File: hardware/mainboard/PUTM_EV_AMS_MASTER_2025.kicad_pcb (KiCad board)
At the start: 4 copper layers, 60 x 100 mm, 236 parts, among them IC1 3.3V/0.5A, IC2 TPS54202HDDCR, IC3 BQ79600PWRQ1, IC4 TLV61046ADBVT, IC6 AMC3330DWER, IC7 AMC3330DWER, IC8 ADC 24bit, IC9 LTC1799, J1 M80-5100642, J10 M300-MV10345M1, J2 M80-5102042, J3 M80-5100842, J4 FTSH-107-01-L-D-K, J5 M80-51004XX, J7 M300-MV10345M1, J8 M80-51004XX, K1 IM07DTS, Q1 DMT6018LDR-7, Q2 DMT6018LDR-7, Q3 DMT6018LDR-7, Q4 SI2347DS-T1-GE3, Q6 2N7002, Q7 DMT6018LDR-7, Q8 2N7002, Q9 2N7002, T1 SM91502ALE, U10 STM32H573RITx, U12 LM393, U13 LM393, U14 LM393, U2 FT230XS, U3 74AUP1G32, U4 TPS2113PWR, U6 MCP2542FD-E/MF, U7 MCP2542FD-E/MF

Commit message: sync
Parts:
- moved TP1 2.25 mm to (139.0, 126.2)
- moved TP4 2.25 mm to (139.0, 128.2)
- moved C47 1.25 mm to (133.8, 88.2)
- moved TP11 1.03 mm to (119.0, 117.0)
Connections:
- J2 pad 12: /CHARGER_DETECTION -> VBUS+
- J2 pad 13: /AIR_P_DETECTION -> /CHARGER_DETECTION
- J2 pad 14: /AIR_PRE_DETECTION -> /AIR_P_DETECTION
- J2 pad 15: /AIR_M_DETECTION -> /AIR_PRE_DETECTION
- J2 pad 16: unconnected-(J2-Pad16) -> /AIR_M_DETECTION
- J2 pad 17: VBUS+ -> +8V
- J2 pad 18: TSMS -> /SAFETY_IN
- J2 pad 7: /SAFETY_OUT -> GND
- J2 pad 8: /SAFETY_IN -> /SAFETY_OUT
- J2 pad 9: +8V -> TSMS
- R49 pad 2: TSMS -> /SDC_AIRS
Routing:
- net /ADC_MOSI: track 0.00 -> 41.1 mm, vias 0 -> 2
- net /~{CS_MISO}: track 0.00 -> 40.5 mm, vias 0 -> 2
- net /ADC_SCK: track 0.00 -> 39.8 mm, vias 0 -> 2
- net /ADC_MISO: track 2.79 -> 42.0 mm, vias 1 -> 2
- net /~{ADC_DRY}: track 0.00 -> 35.4 mm, vias 0 -> 2
- net /UCTX: track 0.00 -> 27.1 mm
- net /UCRX: track 0.00 -> 24.3 mm
- net /ADC/ACU_V-: track 0.00 -> 20.7 mm
- net /~{FLT}: track 7.02 -> 27.7 mm, vias 1 -> 2
- net /UTX: track 0.00 -> 20.6 mm
- net /ADC/ACU_V+: track 0.00 -> 20.6 mm
- net /SDC_AIRS: track 24.1 -> 42.2 mm
- net /URX: track 0.00 -> 16.7 mm
- net /FAN2-: track 4.63 -> 18.9 mm
- net /FAN1-: track 3.47 -> 16.9 mm
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- added copper zone on In2.Cu, net +3.3VA
- added copper zone on In2.Cu, net +3.3VMCU
- added copper zone on In2.Cu, net +5VA

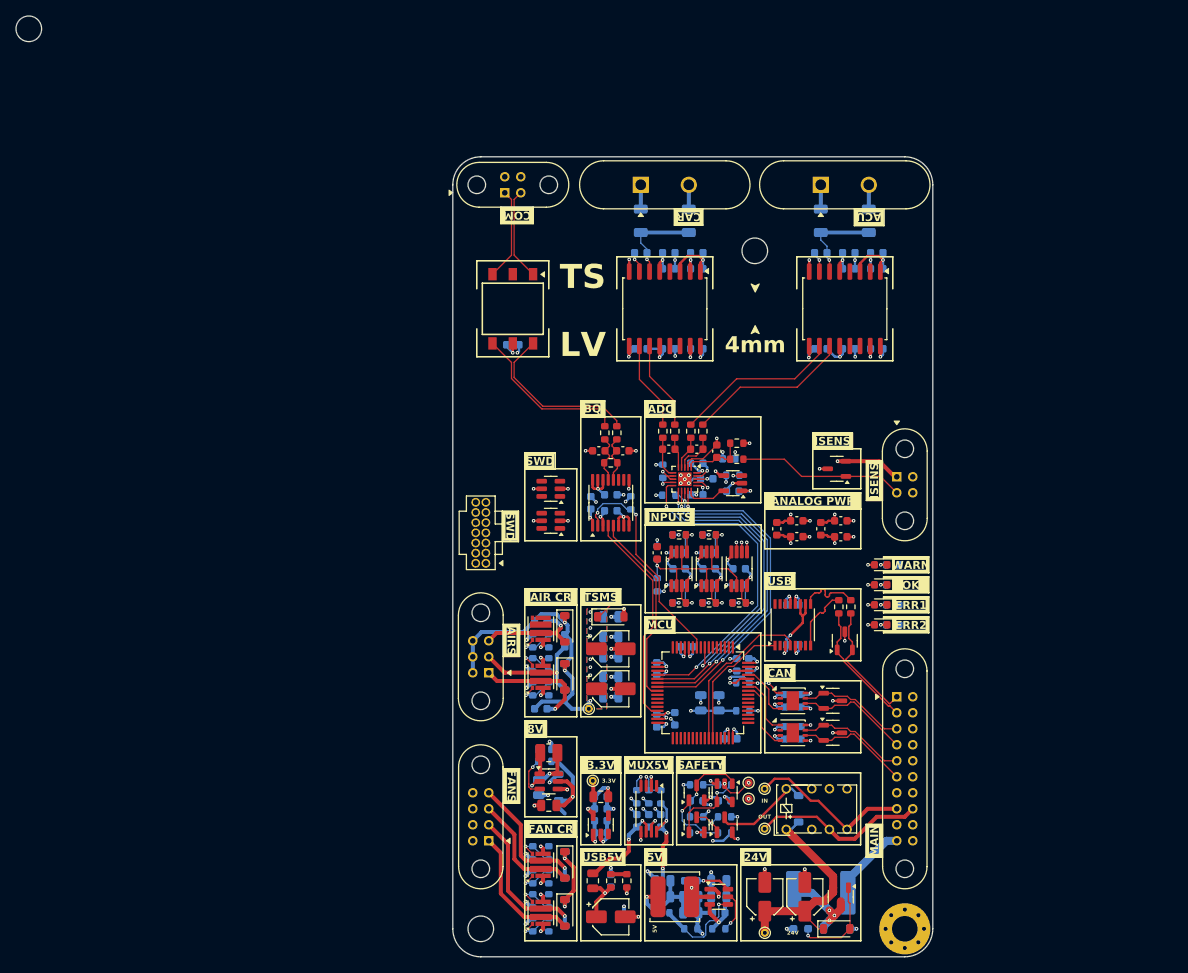
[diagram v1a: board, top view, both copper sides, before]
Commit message: hardware routing done, only touch ups will be needed if the board is aproved
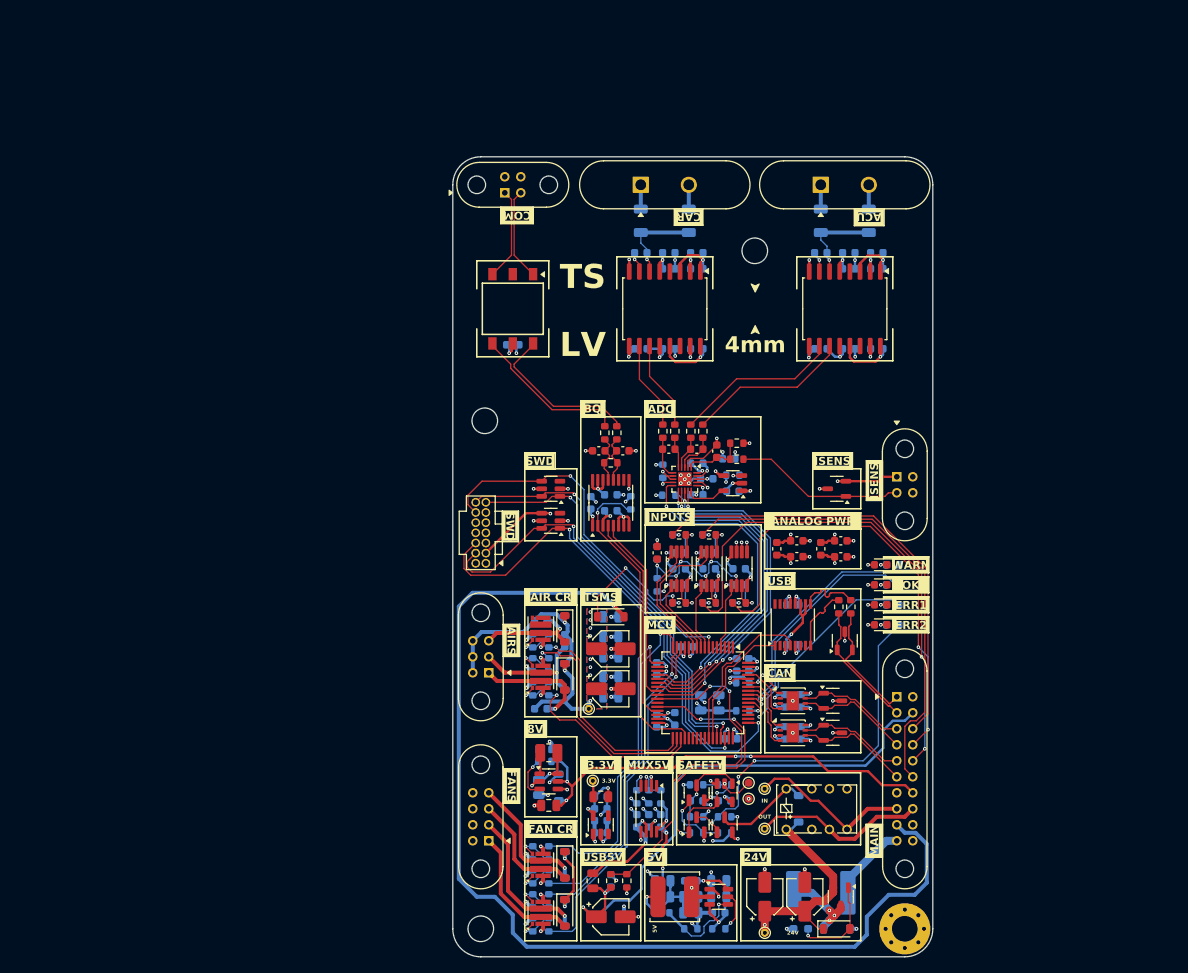
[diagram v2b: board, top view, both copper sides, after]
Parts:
- moved H1 75.2 mm to (106.0, 81.0)
- moved C19 2.50 mm to (145.0, 98.0)
- moved C20 2.50 mm to (145.0, 96.0)
- moved C4 2.50 mm to (150.5, 98.0)
- moved C5 2.50 mm to (150.5, 96.0)
- moved D23 2.50 mm to (150.0, 89.5)
- moved FB1 2.50 mm to (148.0, 97.0)
- moved FB2 2.50 mm to (142.5, 97.0)
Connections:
- C10 pad 2: +5VISO -> +5VIO
- C49 pad 1: +5VIO -> +3.3VIO
- C50 pad 1: +5VIO -> +3.3VIO
- C58 pad 1: +5VIO -> +3.3VIO
- C8 pad 2: +3.3VIO -> +5VIO
- C9 pad 2: +5VISO -> +5VIO
- C93 pad 2: +5VISO -> +5VIO
- C98 pad 2: +5VISO -> +5VIO
- D21 pad 1: /SWDIO -> /UART_RX
- D21 pad 3: /SWCLK -> unconnected-(D21-A-Pad3)
- D22 pad 1: /UART_RX -> /SWCLK
- D22 pad 3: +3.3VIO -> unconnected-(D22-A-Pad3)
- D22 pad 4: unconnected-(D22-A-Pad4) -> +3.3VIO
- D22 pad 6: unconnected-(D22-A-Pad6) -> /SWDIO
- IC6 pad 12: +5VISO -> +5VIO
- IC7 pad 12: +5VISO -> +5VIO
- Q8 pad 3: /AMSERR -> /AMS_ERROR
- Q9 pad 1: /AMSERR -> /AMS_ERROR
- R12 pad 1: +3.3VIO -> +5VIO
- R13 pad 1: /AMSERR -> /AMS_ERROR
- R13 pad 2: +3.3VIO -> +5VIO
- U10 pad 10: /~{FLT} -> /AMD
- U10 pad 11: unconnected-(U10-PC3-Pad11) -> /DCH
- U10 pad 25: unconnected-(U10-PC5-Pad25) -> /~{ADC_DRY}
- U10 pad 27: /DETERR -> unconnected-(U10-PB1-Pad27)
- U10 pad 28: /AMSERR -> /DETERR
- U10 pad 33: /SAM -> /SAE
- U10 pad 35: /SAE -> /SAM
- U10 pad 36: unconnected-(U10-PB15-Pad36) -> /~{FLT}
- U10 pad 37: /AED -> unconnected-(U10-PC6-Pad37)
- U10 pad 38: /AMD -> unconnected-(U10-PC7-Pad38)
- U10 pad 39: /APD -> unconnected-(U10-PC8-Pad39)
- U10 pad 4: unconnected-(U10-PC15-Pad4) -> /APD
- U10 pad 40: /CD -> unconnected-(U10-PC9-Pad40)
- U10 pad 41: /T -> unconnected-(U10-PA8-Pad41)
- U10 pad 8: /~{ADC_DRY} -> /AED
- U10 pad 9: unconnected-(U10-PC1-Pad9) -> /CTSMS
- U12 pad 1: /T -> /CTSMS
- U12 pad 7: /CD -> /DCH
- U12 pad 8: +5VIO -> +3.3VIO
- U13 pad 8: +5VIO -> +3.3VIO
- U14 pad 8: +5VIO -> +3.3VIO
- U3 pad 5: +3.3VIO -> +5VIO
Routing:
- net TSMS: track 1.00 -> 134.2 mm
- net /SWCLK: track 0.00 -> 64.2 mm, vias 0 -> 2
- net /AIR_PRE_DETECTION: track 0.00 -> 63.7 mm, vias 0 -> 2
- net VBUS+: track 7.26 -> 67.7 mm, vias 1 -> 2
- net /AIR_M_DETECTION: track 0.00 -> 58.8 mm
- net /AIR_P_DETECTION: track 0.00 -> 57.9 mm, vias 0 -> 2
- net /CHARGER_DETECTION: track 0.00 -> 56.3 mm
- net /SWDIO: track 0.00 -> 56.0 mm, vias 0 -> 2
- net /UART_TX: track 0.00 -> 53.2 mm, vias 0 -> 2
- net /UART_RX: track 0.00 -> 50.2 mm, vias 0 -> 2
- net /NRST: track 0.00 -> 46.6 mm, vias 0 -> 2
- net /AMS_ERROR: track 0.00 -> 46.3 mm, vias 0 -> 3
- net /FC1: track 0.00 -> 44.1 mm, vias 0 -> 1
- net /DETVUSB: track 2.00 -> 44.7 mm, vias 0 -> 2
- net /FC3: track 0.00 -> 42.2 mm, vias 0 -> 1
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- added copper zone on In2.Cu, net +24V
- added copper zone on In2.Cu, net +5VIO
- added copper zone on In2.Cu, net /IsolationBarrier/CAR_GND
- added copper zone on In2.Cu, net GND

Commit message: v3.3
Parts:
- moved G*** 64.6 mm to (147.5, 89.0)
- moved D7 1.48 mm to (143.8, 129.5), turned to 180 degrees
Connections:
- U14 pad 6: GND -> +3.3VIO
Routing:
- net Net-(D5-A): track 11.9 -> 15.3 mm
- net +24V: track 46.4 -> 47.8 mm
- net /Safety/RELAY-: track 11.6 -> 12.9 mm
- net +3.3VIO: track 40.8 -> 42.0 mm, vias 20 -> 21
- net GND: track 180.6 -> 179.5 mm, vias 128 -> 127

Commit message: isolation with every thing
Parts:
- removed C15, C30, C31, C51, C61, C62, C69: 22uF, Capacitor_SMD:C_0805_2012Metric
- removed C32, C33, C37, C38, C49, C50, C58, C76: 100nF, Capacitor_SMD:C_0603_1608Metric
- removed C63, C64: 22uF, Capacitor_SMD:CP_Elec_4x5.8
- removed D15, D7: 60V/0.5/3A, Diode_SMD:D_SOD-123
- removed D20: 8V, Diode_SMD:D_SOD-123
- removed IC4: TLV61046ADBVT, Package_TO_SOT_SMD:SOT-23-6
- removed K1: IM07DTS, Samacsys:IM23TS
- removed L1: 10uH, Inductor_SMD:L_1008_2520Metric
- removed R41, R42: 10k, Resistor_SMD:R_0603_1608Metric
- removed R49, R53, R63, R68, R70: 100k, Resistor_SMD:R_0603_1608Metric
- removed R55: 649k, Resistor_SMD:R_0603_1608Metric
- removed R62: 71.5k, Resistor_SMD:R_0603_1608Metric
- removed TP11, TP17, TP18: TestPoint_Small, TestPoint:TestPoint_THTPad_D1.0mm_Drill0.5mm
- removed U12, U13, U14: LM393, Package_SO:VSSOP-8_3x3mm_P0.65mm
- removed U6, U7: MCP2542FD-E/MF, Package_DFN_QFN:DFN-8-1EP_3x3mm_P0.65mm_EP1.55x2.4mm
- added C96: 1nF, Capacitor_SMD:C_0603_1608Metric, F.Cu at (189.2, 99.2)
- added D25: 3.6V/400W, Package_TO_SOT_SMD:SOT-23-6, F.Cu at (182.6, 100.4)
- added D26: 3.6V/400W, Package_TO_SOT_SMD:SOT-23-6, F.Cu at (182.6, 105.0)
- added D27: 5.3V/400W, Package_TO_SOT_SMD:SOT-23-3, F.Cu at (181.0, 135.6)
- added R15: 27, Resistor_SMD:R_0603_1608Metric, F.Cu at (178.0, 99.2)
- added R18: 27, Resistor_SMD:R_0603_1608Metric, F.Cu at (178.0, 101.7)
- added R19: 27, Resistor_SMD:R_0603_1608Metric, F.Cu at (178.0, 104.2)
- added R69: 27, Resistor_SMD:R_0603_1608Metric, F.Cu at (178.0, 106.8)
- added R71: 10k, Resistor_SMD:R_0603_1608Metric, F.Cu at (178.0, 109.3)
- added R72: 50k/.1%, Resistor_SMD:R_0603_1608Metric, F.Cu at (189.2, 101.7)
- added R73: 10k/.1%, Resistor_SMD:R_0603_1608Metric, F.Cu at (189.2, 104.2)
- C91, C92, C93, C94, C95, C98: value 1n -> 1nF
- R17: value 20k -> 27
- R20, R21, R25, R26: value 10k -> 27
- moved C34 41.0 mm to (183.3, 122.4)
- moved C44 41.0 mm to (183.3, 117.4)
- moved D12 41.0 mm to (189.8, 121.9)
- moved R7 41.0 mm to (189.0, 117.6)
- moved R8 41.0 mm to (190.5, 117.6)
- moved U2 41.0 mm to (183.3, 119.9)
- moved C89 1.00 mm to (131.5, 84.5)
- moved C90 1.00 mm to (128.0, 84.5)
- moved R50 1.00 mm to (132.2, 82.3)
- moved R51 1.00 mm to (130.8, 82.3)
- moved R52 1.00 mm to (128.8, 82.3)
- moved R54 1.00 mm to (127.2, 82.3)
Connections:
- C101 pad 2: Net-(U12A-+) -> /CTSMS
- C102 pad 2: Net-(U12B-+) -> /DCH
- C103 pad 2: Net-(U13A-+) -> /AED
- C104 pad 2: Net-(U13B-+) -> /AMD
- C105 pad 2: Net-(U14A-+) -> /APD
- C83 pad 2: /SDC_AIRS -> +24V
- C84 pad 2: /SDC_AIRS -> +24V
- C85 pad 2: /SDC_AIRS -> +24V
- D10 pad 1: /SDC_AIRS -> +24V
- D11 pad 1: /CANFD2+ -> /EX_CANFD2_TX
- D11 pad 2: /CANFD2- -> /EX_CANFD2_RX
- D24 pad 1: /SDC_AIRS -> +24V
- D4 pad 1: /CANFD1+ -> /EX_CANFD1_TX
- D4 pad 2: /CANFD1- -> /EX_CANFD1_RX
- D9 pad 1: /SDC_AIRS -> +24V
- IC8 pad 1: /ADC/I+ -> Net-(IC8-CH0+)
- IC8 pad 3: /ADC/ACU+ -> /ADC/I+
- IC8 pad 4: /ADC/ACU- -> GND
- IC8 pad 5: /ADC/CAR+ -> /ADC/ACU+
- IC8 pad 6: /ADC/CAR- -> /ADC/ACU-
- IC8 pad 7: GND -> /ADC/CAR+
- IC8 pad 8: GND -> /ADC/CAR-
- J1 pad 4: /SDC_AIRS -> +24V
- J1 pad 5: /SDC_AIRS -> +24V
- J1 pad 6: /SDC_AIRS -> +24V
- J2 pad 17: +8V -> +3.3VIO
- J2 pad 18: /SAFETY_IN -> +5VIO
- J2 pad 19: GND -> unconnected-(J2-Pad19)
- J2 pad 3: /CANFD1+ -> /EX_CANFD1_RX
- J2 pad 4: /CANFD1- -> /EX_CANFD1_TX
- J2 pad 5: /CANFD2+ -> /EX_CANFD2_RX
- J2 pad 6: /CANFD2- -> /EX_CANFD2_TX
- J2 pad 7: GND -> /TSMS_DETECTION
- J2 pad 8: /SAFETY_OUT -> unconnected-(J2-Pad8)
- J2 pad 9: TSMS -> /ERROR_RELAY-
- Q9 pad 3: /Safety/RELAY- -> /ERROR_RELAY-
- R17 pad 1: +3.3VIO -> /CTSMS
- R17 pad 2: /Connectivity/REF -> /TSMS_DETECTION
- R20 pad 1: GND -> /DCH
- R20 pad 2: Net-(U12A-+) -> /CHARGER_DETECTION
- R21 pad 1: GND -> /AED
- R21 pad 2: Net-(U12B-+) -> /AIR_PRE_DETECTION
- R25 pad 1: GND -> /AMD
- R25 pad 2: Net-(U13A-+) -> /AIR_M_DETECTION
- R26 pad 1: /Connectivity/REF -> /APD
- R26 pad 2: GND -> /AIR_P_DETECTION
- U10 pad 2: unconnected-(U10-PC13-Pad2) -> /Connectivity/~{FTDI_RST}
- U2 pad 11: /Connectivity/+3.3VFTDI -> /Connectivity/~{FTDI_RST}
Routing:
- net TSMS: track 134.2 -> 0.00 mm, vias 1 -> 0
- net /ERROR_RELAY-: track 0.00 -> 130.1 mm
- net (no net): track 0.00 -> 88.8 mm
- net +8V: track 56.4 -> 0.00 mm, vias 4 -> 0
- net /SDC_AIRS: track 56.0 -> 0.00 mm, vias 12 -> 0
- net GND: track 179.5 -> 144.5 mm, vias 127 -> 103
- net +24V: track 47.8 -> 74.5 mm, vias 4 -> 7
- net /Connectivity/REF: track 24.2 -> 0.00 mm, vias 6 -> 0
- net /SAFETY_IN: track 21.8 -> 0.00 mm
- net /SAFETY_OUT: track 20.7 -> 0.00 mm
- net /CANFD1-: track 13.9 -> 0.00 mm
- net /CANFD2-: track 13.9 -> 0.00 mm
- net /CANFD2+: track 13.2 -> 0.00 mm
- net /CANFD1+: track 13.2 -> 0.00 mm
- net /Safety/RELAY-: track 12.9 -> 0.00 mm
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- removed copper zone on B.Cu, net /SDC_AIRS
- removed copper zone on F.Cu, net /SDC_AIRS
- removed copper zone on In2.Cu, net GND
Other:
- board text removed: "8V"
- board text removed: "TSMS"
